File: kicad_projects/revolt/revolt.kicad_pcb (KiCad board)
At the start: 2 copper layers, 143.5 x 111.4 mm, 68 parts

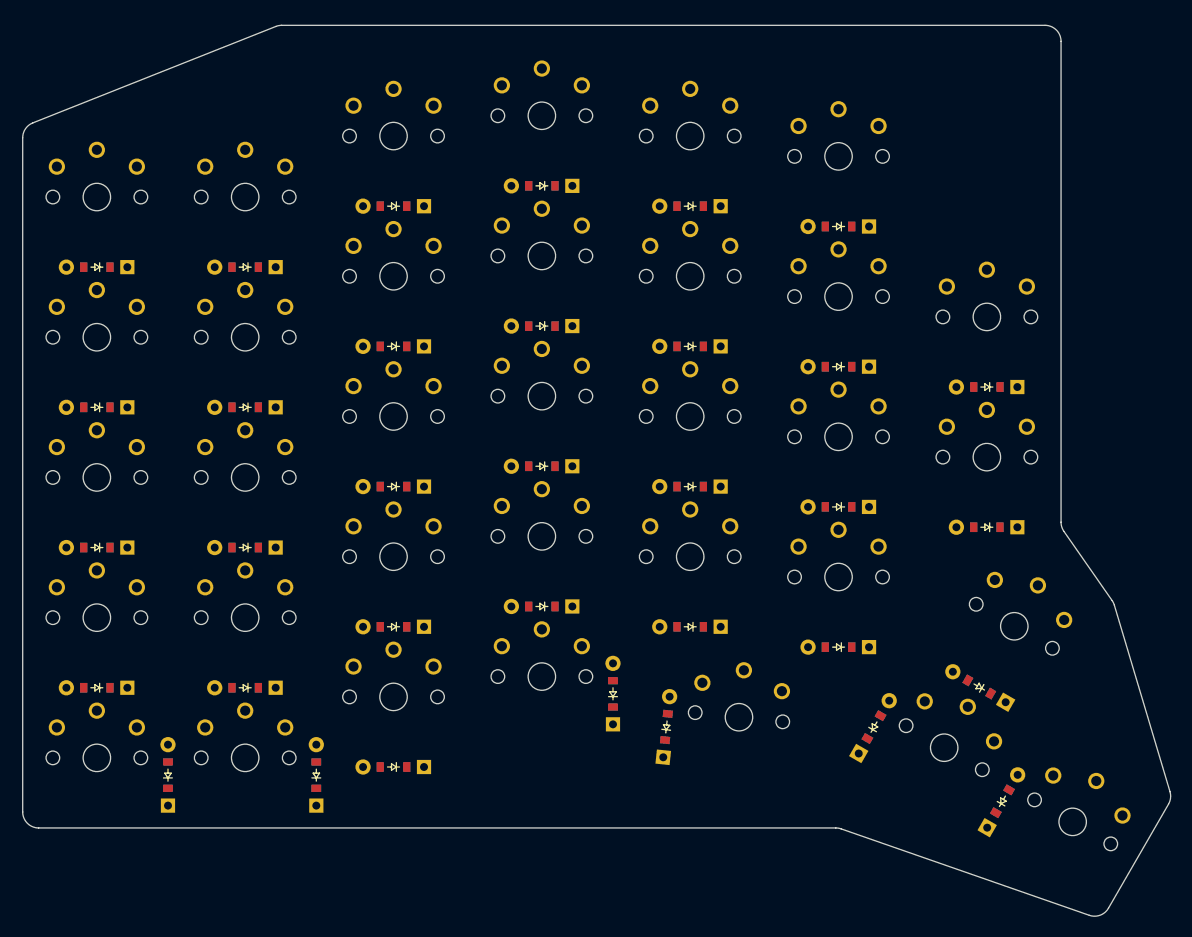
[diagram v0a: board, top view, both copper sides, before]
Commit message: add matrix to the schematic, minus the net names
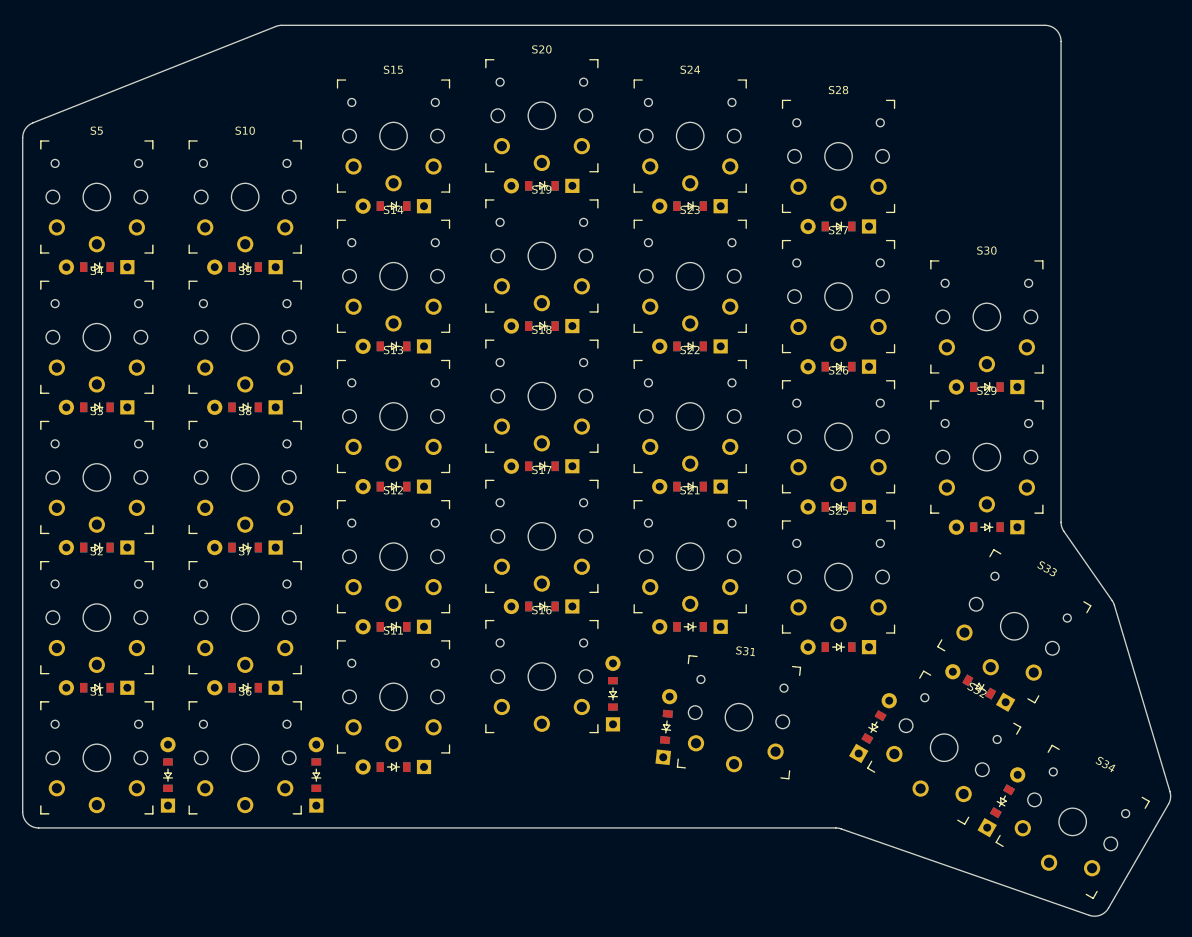
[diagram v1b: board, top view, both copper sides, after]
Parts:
- S1, S10, S11, S12, S13, S14, S15, S16, S17, S18, S19, S2, S20, S21, S22, S23, S24, S25, S26, S27, S28, S29, S3, S30, S31, S32, S33, S34, S4, S5, S6, S7, S8, S9: footprint PG1350 -> keyswitches:SW_PG1350_reversible

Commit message: Update the diode numbers
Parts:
- D1: renamed from D29; value (none) -> ~
- D10: renamed from D8; value (none) -> ~
- D11: renamed from D9; value (none) -> ~
- D12: renamed from D10; value (none) -> ~
- D13: renamed from D11; value (none) -> ~
- D14: renamed from D12; value (none) -> ~
- D15: renamed from D13; value (none) -> ~
- D16: renamed from D31; value (none) -> ~
- D17: renamed from D14; value (none) -> ~
- D18: renamed from D15; value (none) -> ~
- D19: renamed from D16; value (none) -> ~
- D2: renamed from D1; value (none) -> ~
- D20: renamed from D17; value (none) -> ~
- D21: renamed from D18; value (none) -> ~
- D22: renamed from D19; value (none) -> ~
- D23: renamed from D20; value (none) -> ~
- D24: renamed from D21; value (none) -> ~
- D25: renamed from D22; value (none) -> ~
- D26: renamed from D23; value (none) -> ~
- D27: renamed from D24; value (none) -> ~
- D28: renamed from D25; value (none) -> ~
- D29: renamed from D26; value (none) -> ~
- D3: renamed from D2; value (none) -> ~
- D30: renamed from D27; value (none) -> ~
- D31: renamed from D32; value (none) -> ~
- D32: renamed from D33; value (none) -> ~
- D33: renamed from D28; value (none) -> ~
- D34, S1, S10, S11, S12, S13, S14, S15, S16, S17, S18, S19, S2, S20, S21, S22, S23, S24, S25, S26, S27, S28, S29, S3, S30, S31, S32, S33, S34, S4, S5, S6, S7, S8, S9: value (none) -> ~
- D4: renamed from D3; value (none) -> ~
- D5: renamed from D4; value (none) -> ~
- D6: renamed from D30; value (none) -> ~
- D7: renamed from D5; value (none) -> ~
- D8: renamed from D6; value (none) -> ~
- D9: renamed from D7; value (none) -> ~
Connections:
- net COL0 renamed /COL0
- net COL1 renamed /COL1
- net COL2 renamed /COL2
- net COL3 renamed /COL3
- net COL4 renamed /COL4
- net COL5 renamed /COL5
- net COL6 renamed /COL6
- net far_home renamed /far_home
- D1 pad 1: ROW4 -> /ROW0
- D1 pad 2: outer_mod -> /bonus_home
- D10 pad 1: ROW0 -> /ROW0
- D10 pad 2: pinky_num -> /pinky_num
- D11 pad 1: ROW4 -> /ROW0
- D11 pad 2: ring_mod -> /ring_mod
- D12 pad 1: ROW3 -> /ROW2
- D12 pad 2: ring_bottom -> /ring_bottom
- D13 pad 1: ROW2 -> /ROW4
- D13 pad 2: ring_home -> /ring_mod
- D14 pad 1: ROW1 -> /ROW0
- D14 pad 2: ring_top -> /ring_bottom
- D15 pad 1: ROW0 -> /ROW0
- D15 pad 2: ring_num -> /ring_home
- D16 pad 1: ROW4 -> /ROW4
- D16 pad 2: middle_mod -> /index_mod
- D17 pad 1: ROW3 -> /ROW0
- D17 pad 2: middle_bottom -> /ring_top
- D18 pad 1: ROW2 -> /ROW2
- D18 pad 2: middle_home -> /middle_home
- D19 pad 1: ROW1 -> /ROW4
- D19 pad 2: middle_top -> /middle_top
- D2 pad 1: ROW3 -> /ROW4
- D2 pad 2: outer_bottom -> /outer_mod
- D20 pad 1: ROW0 -> /ROW0
- D20 pad 2: middle_num -> /middle_bottom
- D21 pad 1: ROW3 -> /ROW0
- D21 pad 2: index_bottom -> /middle_home
- D22 pad 1: ROW2 -> /ROW0
- D22 pad 2: index_home -> /middle_top
- D23 pad 1: ROW1 -> /ROW2
- D23 pad 2: index_top -> /index_top
- D24 pad 1: ROW0 -> /ROW0
- D24 pad 2: index_num -> /index_num
- D25 pad 1: ROW3 -> /ROW0
- D25 pad 2: inner_bottom -> /inner_bottom
- D26 pad 1: ROW2 -> /ROW0
- D26 pad 2: inner_home -> /inner_home
- D27 pad 1: ROW1 -> /ROW2
- D27 pad 2: inner_top -> /index_num
- D28 pad 1: ROW0 -> /ROW0
- D28 pad 2: inner_num -> /inner_num
- D29 pad 1: ROW2 -> /ROW0
- D29 pad 2: bonus_home -> /inner_home
- D3 pad 1: ROW2 -> /ROW0
- D3 pad 2: outer_home -> /outer_home
- D30 pad 1: ROW1 -> /ROW0
- D30 pad 2: bonus_top -> /inner_top
- D31 pad 1: ROW4 -> /ROW4
- D31 pad 2: index_mod -> /index_mod
- D32 pad 1: ROW4 -> /ROW0
- D32 pad 2: close_home -> /close_top
- D33 pad 1: ROW3 -> /ROW2
- D33 pad 2: close_top -> /close_top
- D34 pad 1: ROW4 -> /ROW4
- D4 pad 1: ROW1 -> /ROW0
- D4 pad 2: outer_top -> /outer_top
- D5 pad 1: ROW0 -> /ROW0
- D5 pad 2: outer_num -> /outer_num
- D6 pad 1: ROW4 -> /ROW0
- D6 pad 2: pinky_mod -> /bonus_top
- D7 pad 1: ROW3 -> /ROW2
- D7 pad 2: pinky_bottom -> /pinky_bottom
- D8 pad 1: ROW2 -> /ROW4
- D8 pad 2: pinky_home -> /pinky_mod
- D9 pad 1: ROW1 -> /ROW0
- D9 pad 2: pinky_top -> /pinky_bottom
- S1 pad 2: outer_mod -> /outer_mod
- S10 pad 2: pinky_num -> /ring_bottom
- S11 pad 2: ring_mod -> /ring_mod
- S12 pad 2: ring_bottom -> /ring_bottom
- S13 pad 2: ring_home -> /ring_home
- S14 pad 2: ring_top -> /ring_top
- S15 pad 2: ring_num -> /middle_home
- S16 pad 2: middle_mod -> /middle_top
- S17 pad 2: middle_bottom -> /middle_bottom
- S18 pad 2: middle_home -> /middle_home
- S19 pad 2: middle_top -> /middle_top
- S2 pad 2: outer_bottom -> /outer_home
- S20 pad 2: middle_num -> /index_top
- S21 pad 2: index_bottom -> /index_num
- S22 pad 2: index_home -> /inner_bottom
- S23 pad 2: index_top -> /inner_home
- S24 pad 2: index_num -> /index_num
- S25 pad 2: inner_bottom -> /inner_num
- S26 pad 2: inner_home -> /inner_home
- S27 pad 2: inner_top -> /inner_top
- S28 pad 2: inner_num -> /close_top
- S29 pad 2: bonus_home -> /bonus_home
- S3 pad 2: outer_home -> /outer_top
- S30 pad 2: bonus_top -> /bonus_top
- S31 pad 2: index_mod -> /index_mod
- S32 pad 2: close_home -> /index_mod
- S33 pad 2: close_top -> /close_top
- S4 pad 2: outer_top -> /outer_num
- S5 pad 2: outer_num -> /pinky_bottom
- S6 pad 2: pinky_mod -> /pinky_mod
- S7 pad 2: pinky_bottom -> /pinky_bottom
- S8 pad 2: pinky_home -> /pinky_num
- S9 pad 2: pinky_top -> /ring_mod

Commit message: fix pcb diode numbers
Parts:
- D1, D10, D11, D12, D13, D14, D15, D16, D17, D18, D19, D2, D20, D21, D22, D23, D24, D25, D26, D27, D28, D29, D3, D30, D31, D32, D33, D34, D4, D5, D6, D7, D8, D9, S1, S10, S11, S12, S13, S14, S15, S16, S17, S18, S19, S2, S20, S21, S22, S23, S24, S25, S26, S27, S28, S29, S3, S30, S31, S32, S33, S34, S4, S5, S6, S7, S8, S9: value ~ -> (none)
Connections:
- net /COL0 renamed COL0
- net /COL1 renamed COL1
- net /COL2 renamed COL2
- net /COL3 renamed COL3
- net /COL4 renamed COL4
- net /COL5 renamed COL5
- net /COL6 renamed COL6
- net /far_home renamed far_home
- D1 pad 1: /ROW0 -> ROW4
- D1 pad 2: /bonus_home -> outer_mod
- D10 pad 1: /ROW0 -> ROW0
- D10 pad 2: /pinky_num -> pinky_num
- D11 pad 1: /ROW0 -> ROW4
- D11 pad 2: /ring_mod -> ring_mod
- D12 pad 1: /ROW2 -> ROW3
- D12 pad 2: /ring_bottom -> ring_bottom
- D13 pad 1: /ROW4 -> ROW2
- D13 pad 2: /ring_mod -> ring_home
- D14 pad 1: /ROW0 -> ROW1
- D14 pad 2: /ring_bottom -> ring_top
- D15 pad 1: /ROW0 -> ROW0
- D15 pad 2: /ring_home -> ring_num
- D16 pad 1: /ROW4 -> ROW4
- D16 pad 2: /index_mod -> middle_mod
- D17 pad 1: /ROW0 -> ROW3
- D17 pad 2: /ring_top -> middle_bottom
- D18 pad 1: /ROW2 -> ROW2
- D18 pad 2: /middle_home -> middle_home
- D19 pad 1: /ROW4 -> ROW1
- D19 pad 2: /middle_top -> middle_top
- D2 pad 1: /ROW4 -> ROW3
- D2 pad 2: /outer_mod -> outer_bottom
- D20 pad 1: /ROW0 -> ROW0
- D20 pad 2: /middle_bottom -> middle_num
- D21 pad 1: /ROW0 -> ROW3
- D21 pad 2: /middle_home -> index_bottom
- D22 pad 1: /ROW0 -> ROW2
- D22 pad 2: /middle_top -> index_home
- D23 pad 1: /ROW2 -> ROW1
- D23 pad 2: /index_top -> index_top
- D24 pad 1: /ROW0 -> ROW0
- D24 pad 2: /index_num -> index_num
- D25 pad 1: /ROW0 -> ROW3
- D25 pad 2: /inner_bottom -> inner_bottom
- D26 pad 1: /ROW0 -> ROW2
- D26 pad 2: /inner_home -> inner_home
- D27 pad 1: /ROW2 -> ROW1
- D27 pad 2: /index_num -> inner_top
- D28 pad 1: /ROW0 -> ROW0
- D28 pad 2: /inner_num -> inner_num
- D29 pad 1: /ROW0 -> ROW2
- D29 pad 2: /inner_home -> bonus_home
- D3 pad 1: /ROW0 -> ROW2
- D3 pad 2: /outer_home -> outer_home
- D30 pad 1: /ROW0 -> ROW1
- D30 pad 2: /inner_top -> bonus_top
- D31 pad 1: /ROW4 -> ROW4
- D31 pad 2: /index_mod -> index_mod
- D32 pad 1: /ROW0 -> ROW4
- D32 pad 2: /close_top -> close_home
- D33 pad 1: /ROW2 -> ROW3
- D33 pad 2: /close_top -> close_top
- D34 pad 1: /ROW4 -> ROW4
- D4 pad 1: /ROW0 -> ROW1
- D4 pad 2: /outer_top -> outer_top
- D5 pad 1: /ROW0 -> ROW0
- D5 pad 2: /outer_num -> outer_num
- D6 pad 1: /ROW0 -> ROW4
- D6 pad 2: /bonus_top -> pinky_mod
- D7 pad 1: /ROW2 -> ROW3
- D7 pad 2: /pinky_bottom -> pinky_bottom
- D8 pad 1: /ROW4 -> ROW2
- D8 pad 2: /pinky_mod -> pinky_home
- D9 pad 1: /ROW0 -> ROW1
- D9 pad 2: /pinky_bottom -> pinky_top
- S1 pad 2: /outer_mod -> outer_mod
- S10 pad 2: /ring_bottom -> pinky_num
- S11 pad 2: /ring_mod -> ring_mod
- S12 pad 2: /ring_bottom -> ring_bottom
- S13 pad 2: /ring_home -> ring_home
- S14 pad 2: /ring_top -> ring_top
- S15 pad 2: /middle_home -> ring_num
- S16 pad 2: /middle_top -> middle_mod
- S17 pad 2: /middle_bottom -> middle_bottom
- S18 pad 2: /middle_home -> middle_home
- S19 pad 2: /middle_top -> middle_top
- S2 pad 2: /outer_home -> outer_bottom
- S20 pad 2: /index_top -> middle_num
- S21 pad 2: /index_num -> index_bottom
- S22 pad 2: /inner_bottom -> index_home
- S23 pad 2: /inner_home -> index_top
- S24 pad 2: /index_num -> index_num
- S25 pad 2: /inner_num -> inner_bottom
- S26 pad 2: /inner_home -> inner_home
- S27 pad 2: /inner_top -> inner_top
- S28 pad 2: /close_top -> inner_num
- S29 pad 2: /bonus_home -> bonus_home
- S3 pad 2: /outer_top -> outer_home
- S30 pad 2: /bonus_top -> bonus_top
- S31 pad 2: /index_mod -> index_mod
- S32 pad 2: /index_mod -> close_home
- S33 pad 2: /close_top -> close_top
- S4 pad 2: /outer_num -> outer_top
- S5 pad 2: /pinky_bottom -> outer_num
- S6 pad 2: /pinky_mod -> pinky_mod
- S7 pad 2: /pinky_bottom -> pinky_bottom
- S8 pad 2: /pinky_num -> pinky_home
- S9 pad 2: /ring_mod -> pinky_top

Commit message: fixed pcb and schematic
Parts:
- D1, D10, D11, D12, D13, D14, D15, D16, D17, D18, D19, D2, D20, D21, D22, D23, D24, D25, D26, D27, D28, D29, D3, D30, D31, D32, D33, D34, D4, D5, D6, D7, D8, D9, S1, S10, S11, S12, S13, S14, S15, S16, S17, S18, S19, S2, S20, S21, S22, S23, S24, S25, S26, S27, S28, S29, S3, S30, S31, S32, S33, S34, S4, S5, S6, S7, S8, S9: value (none) -> ~
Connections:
- net COL0 renamed /COL0
- net COL1 renamed /COL1
- net COL2 renamed /COL2
- net COL3 renamed /COL3
- net COL4 renamed /COL4
- net COL5 renamed /COL5
- net COL6 renamed /COL6
- net ROW0 renamed /ROW0
- net ROW1 renamed /ROW1
- net ROW2 renamed /ROW2
- net ROW3 renamed /ROW3
- net ROW4 renamed /ROW4
- net bonus_home renamed Net-(D29-A)
- net bonus_top renamed Net-(D30-A)
- net close_home renamed Net-(D32-A)
- net close_top renamed Net-(D33-A)
- net far_home renamed Net-(D34-A)
- net index_bottom renamed Net-(D21-A)
- net index_home renamed Net-(D22-A)
- net index_mod renamed Net-(D31-A)
- net index_num renamed Net-(D24-A)
- net index_top renamed Net-(D23-A)
- net inner_bottom renamed Net-(D25-A)
- net inner_home renamed Net-(D26-A)
- net inner_num renamed Net-(D28-A)
- net inner_top renamed Net-(D27-A)
- net middle_bottom renamed Net-(D17-A)
- net middle_home renamed Net-(D18-A)
- net middle_mod renamed Net-(D16-A)
- net middle_num renamed Net-(D20-A)
- net middle_top renamed Net-(D19-A)
- net outer_bottom renamed Net-(D2-A)
- net outer_home renamed Net-(D3-A)
- net outer_mod renamed Net-(D1-A)
- net outer_num renamed Net-(D5-A)
- net outer_top renamed Net-(D4-A)
- net pinky_bottom renamed Net-(D7-A)
- net pinky_home renamed Net-(D8-A)
- net pinky_mod renamed Net-(D6-A)
- net pinky_num renamed Net-(D10-A)
- net pinky_top renamed Net-(D9-A)
- net ring_bottom renamed Net-(D12-A)
- net ring_home renamed Net-(D13-A)
- net ring_mod renamed Net-(D11-A)
- net ring_num renamed Net-(D15-A)
- net ring_top renamed Net-(D14-A)
